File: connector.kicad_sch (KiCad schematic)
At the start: 7 parts, among them J3 Conn_01x02, J4 Conn_02x20_Counter_Clockwise

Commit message: Populate Board
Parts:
- removed J3: Conn_01x02, TerminalBlock_Phoenix:TerminalBlock_Phoenix_PT-1,5-2-5.0-H_1x02_P5.00mm_Horizontal, symbol Connector_Generic:Conn_01x02
- removed JP10, JP6, JP7, JP8, JP9: SolderJumper_2_Bridged, Jumper:SolderJumper-2_P1.3mm_Bridged_Pad1.0x1.5mm, symbol Jumper:SolderJumper_2_Bridged
- renumbered J4 to J5
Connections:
- net PROTO-1 is gone; now on net Flex_Sensor: J5.27 (Pin_27)
- net PROTO-2 is gone; now on net FAN-OUT: J5.29 (Pin_29)
- net PROTO-3 is gone; now on net FUELPUMP-OUT: J5.31 (Pin_31)
- net PROTO-4 is gone; now on net TACHO-OUT: J5.33 (Pin_33)
- net PROTO-5 is gone; now on net Clutch_in: J5.35 (Pin_35)
- net HC-1-OUT: now also J5.9 (Pin_9); no longer J5.10 (Pin_10)
- net HC-2-OUT: now also J5.10 (Pin_10); no longer J5.6 (Pin_6)
- net IDLE-OUT: now also J5.11 (Pin_11); no longer J5.8 (Pin_8)
- net INJ-3-OUT: now also J5.6 (Pin_6); no longer J5.7 (Pin_7)
- net INJ-4-OUT: now also J5.7 (Pin_7), J5.8 (Pin_8); no longer J5.11 (Pin_11), J5.9 (Pin_9)
- net VDDA renamed +5VA
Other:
- note added: "To Fix"

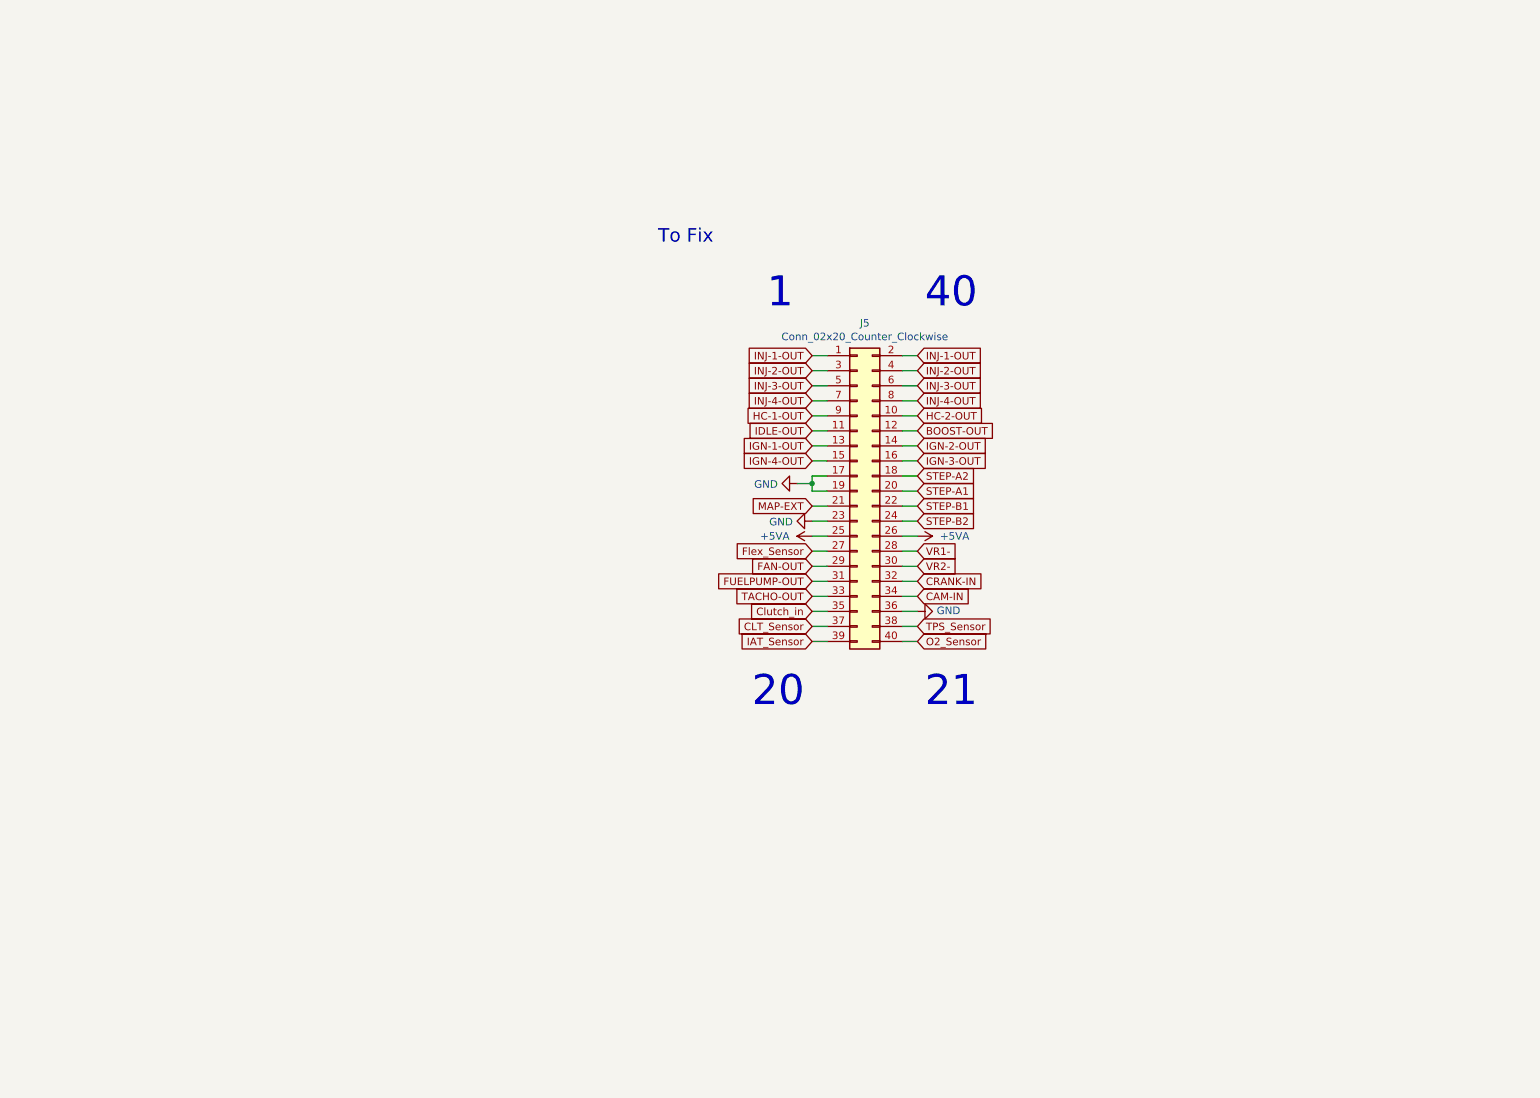
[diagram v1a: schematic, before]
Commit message: Add additional IOs
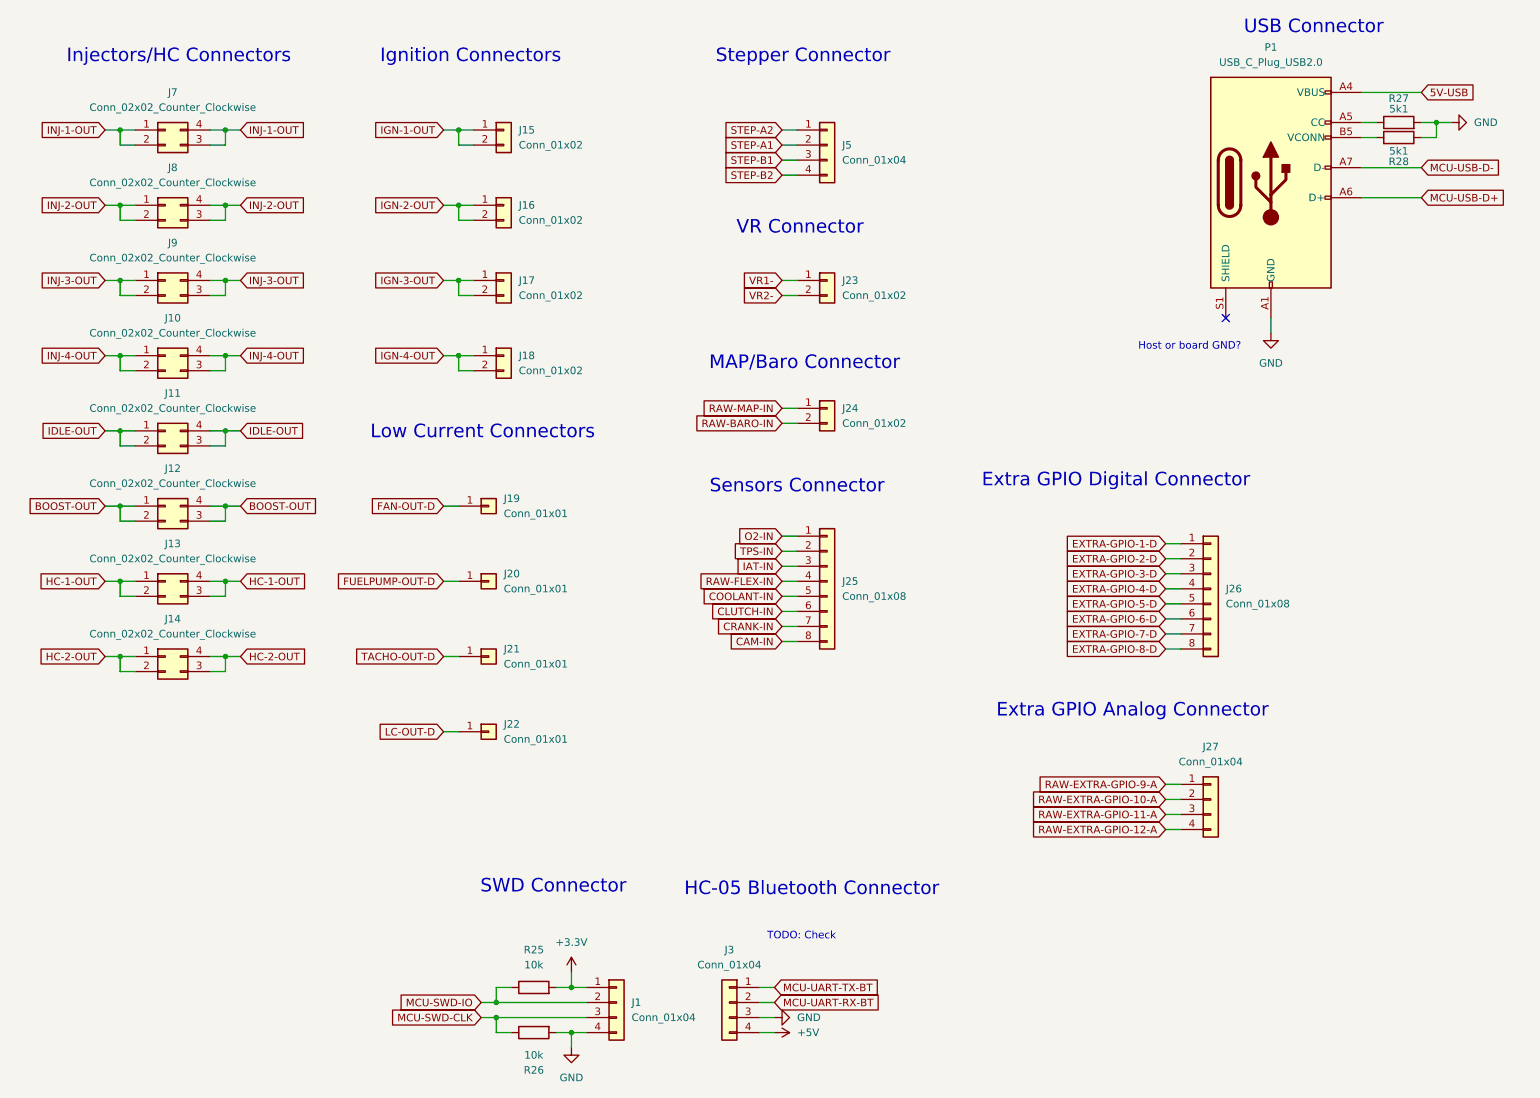
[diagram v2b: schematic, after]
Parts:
- removed J5: Conn_02x20_Counter_Clockwise, Connector_IDC:IDC-Header_2x20_P2.54mm_Vertical, symbol Connector_Generic:Conn_02x20_Odd_Even
- added J1, J27, J3, J5: Conn_01x04, Connector_PinHeader_2.54mm:PinHeader_1x04_P2.54mm_Vertical, symbol Connector_Generic:Conn_01x04
- added J10, J11, J12, J13, J14, J7, J8, J9: Conn_02x02_Counter_Clockwise, Connector_PinHeader_2.54mm:PinHeader_2x02_P2.54mm_Vertical, symbol Connector_Generic:Conn_02x02_Counter_Clockwise
- added J15, J16, J17, J18, J23, J24: Conn_01x02, Connector_PinHeader_2.54mm:PinHeader_1x02_P2.54mm_Vertical, symbol Connector_Generic:Conn_01x02
- added J19, J20, J21, J22: Conn_01x01, Connector_PinHeader_2.54mm:PinHeader_1x01_P2.54mm_Vertical, symbol Connector_Generic:Conn_01x01
- added J25, J26: Conn_01x08, Connector_PinHeader_2.54mm:PinHeader_1x08_P2.54mm_Vertical, symbol Connector_Generic:Conn_01x08
- added P1: USB_C_Plug_USB2.0, Connector_USB:USB_C_Receptacle_Palconn_UTC16-G, symbol Connector:USB_C_Plug_USB2.0
- added R25, R26: 10k, Resistor_SMD:R_0805_2012Metric, symbol Device:R
- added R27, R28: 5k1, Resistor_SMD:R_0805_2012Metric, symbol Device:R
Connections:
- net BOOST-OUT: now also J12.1 (Pin_1), J12.2 (Pin_2), J12.3 (Pin_3), J12.4 (Pin_4)
- net CAM-IN: now also J25.8 (Pin_8)
- net CRANK-IN: now also J25.7 (Pin_7)
- net GND: now also J1.4 (Pin_4), J3.3 (Pin_3), P1.A1 (GND), P1.A12 (GND), P1.B1 (GND), P1.B12 (GND), R26.2, R27.2, R28.1
- net HC-1-OUT: now also J13.1 (Pin_1), J13.2 (Pin_2), J13.3 (Pin_3), J13.4 (Pin_4)
- net HC-2-OUT: now also J14.1 (Pin_1), J14.2 (Pin_2), J14.3 (Pin_3), J14.4 (Pin_4)
- net IDLE-OUT: now also J11.1 (Pin_1), J11.2 (Pin_2), J11.3 (Pin_3), J11.4 (Pin_4)
- net IGN-1-OUT: now also J15.1 (Pin_1), J15.2 (Pin_2)
- net IGN-2-OUT: now also J16.1 (Pin_1), J16.2 (Pin_2)
- net IGN-3-OUT: now also J17.1 (Pin_1), J17.2 (Pin_2)
- net IGN-4-OUT: now also J18.1 (Pin_1), J18.2 (Pin_2)
- net INJ-1-OUT: now also J7.1 (Pin_1), J7.2 (Pin_2), J7.3 (Pin_3), J7.4 (Pin_4)
- net INJ-2-OUT: now also J8.1 (Pin_1), J8.2 (Pin_2), J8.3 (Pin_3), J8.4 (Pin_4)
- net INJ-3-OUT: now also J9.1 (Pin_1), J9.2 (Pin_2), J9.3 (Pin_3), J9.4 (Pin_4)
- net INJ-4-OUT: now also J10.1 (Pin_1), J10.2 (Pin_2), J10.3 (Pin_3), J10.4 (Pin_4)
- net STEP-A1: now also J5.2 (Pin_2)
- net STEP-A2: now also J5.1 (Pin_1)
- net STEP-B1: now also J5.3 (Pin_3)
- net STEP-B2: now also J5.4 (Pin_4)
- net VR1-: now also J23.1 (Pin_1)
- net VR2-: now also J23.2 (Pin_2)
- new net: P1.A5 (CC), R27.1
- new net: P1.B5 (VCONN), R28.2
- new net +3.3V: J1.1 (Pin_1), R25.2
- new net +5V: J3.4 (Pin_4)
- new net 5V-USB: P1.A4 (VBUS), P1.A9 (VBUS), P1.B4 (VBUS), P1.B9 (VBUS)
- new net CLUTCH-IN: J25.6 (Pin_6)
- new net COOLANT-IN: J25.5 (Pin_5)
- new net EXTRA-GPIO-1-D: J26.1 (Pin_1)
- new net EXTRA-GPIO-2-D: J26.2 (Pin_2)
- new net EXTRA-GPIO-3-D: J26.3 (Pin_3)
- new net EXTRA-GPIO-4-D: J26.4 (Pin_4)
- new net EXTRA-GPIO-5-D: J26.5 (Pin_5)
- new net EXTRA-GPIO-6-D: J26.6 (Pin_6)
- new net EXTRA-GPIO-7-D: J26.7 (Pin_7)
- new net EXTRA-GPIO-8-D: J26.8 (Pin_8)
- new net FAN-OUT-D: J19.1 (Pin_1)
- new net FUELPUMP-OUT-D: J20.1 (Pin_1)
- new net IAT-IN: J25.3 (Pin_3)
- new net LC-OUT-D: J22.1 (Pin_1)
- new net MCU-SWD-CLK: J1.3 (Pin_3), R26.1
- new net MCU-SWD-IO: J1.2 (Pin_2), R25.1
- new net MCU-UART-RX-BT: J3.2 (Pin_2)
- new net MCU-UART-TX-BT: J3.1 (Pin_1)
- new net MCU-USB-D+: P1.A6 (D+)
- new net MCU-USB-D-: P1.A7 (D-)
- new net O2-IN: J25.1 (Pin_1)
- new net RAW-BARO-IN: J24.2 (Pin_2)
- new net RAW-EXTRA-GPIO-10-A: J27.2 (Pin_2)
- new net RAW-EXTRA-GPIO-11-A: J27.3 (Pin_3)
- new net RAW-EXTRA-GPIO-12-A: J27.4 (Pin_4)
- new net RAW-EXTRA-GPIO-9-A: J27.1 (Pin_1)
- new net RAW-FLEX-IN: J25.4 (Pin_4)
- new net RAW-MAP-IN: J24.1 (Pin_1)
- new net TACHO-OUT-D: J21.1 (Pin_1)
- new net TPS-IN: J25.2 (Pin_2)
- no-connect marks 0 -> 1
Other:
- note added: "Extra GPIO Analog Connector"
- note added: "Extra GPIO Digital Connector"
- note added: "HC-05 Bluetooth Connector"
- note added: "Host or board GND?"
- note added: "Ignition Connectors"
- note added: "Injectors/HC Connectors"
- note added: "Low Current Connectors"
- note added: "MAP/Baro Connector"
- note added: "SWD Connector"
- note added: "Sensors Connector"
- note added: "Stepper Connector"
- note added: "TODO: Check"
- note added: "USB Connector"
- note added: "VR Connector"
- note removed: "1"
- note removed: "20"
- note removed: "21"
- note removed: "40"
- note removed: "To Fix"

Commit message: Pre MCU switch
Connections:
- net CLUTCH-IN: now also J25.3 (Pin_3); no longer J25.6 (Pin_6)
- net COOLANT-IN: now also J25.6 (Pin_6); no longer J25.5 (Pin_5)
- net IAT-IN: now also J25.2 (Pin_2); no longer J25.3 (Pin_3)
- net O2-IN: now also J25.5 (Pin_5); no longer J25.1 (Pin_1)
- net RAW-FLEX-IN: now also J25.1 (Pin_1); no longer J25.4 (Pin_4)
- net TPS-IN: now also J25.4 (Pin_4); no longer J25.2 (Pin_2)
- net EXTRA-GPIO-1-D renamed MCU-EXTRA-GPIO-1-D
- net EXTRA-GPIO-2-D renamed MCU-EXTRA-GPIO-2-D
- net EXTRA-GPIO-3-D renamed MCU-EXTRA-GPIO-3-D
- net EXTRA-GPIO-4-D renamed MCU-EXTRA-GPIO-4-D
- net EXTRA-GPIO-5-D renamed MCU-EXTRA-GPIO-5-D
- net EXTRA-GPIO-6-D renamed MCU-EXTRA-GPIO-6-D
- net EXTRA-GPIO-7-D renamed MCU-EXTRA-GPIO-7-D
- net EXTRA-GPIO-8-D renamed MCU-EXTRA-GPIO-8-D
- net MCU-UART-RX-BT renamed MCU-UART-BT-RX
- net MCU-UART-TX-BT renamed MCU-UART-BT-TX

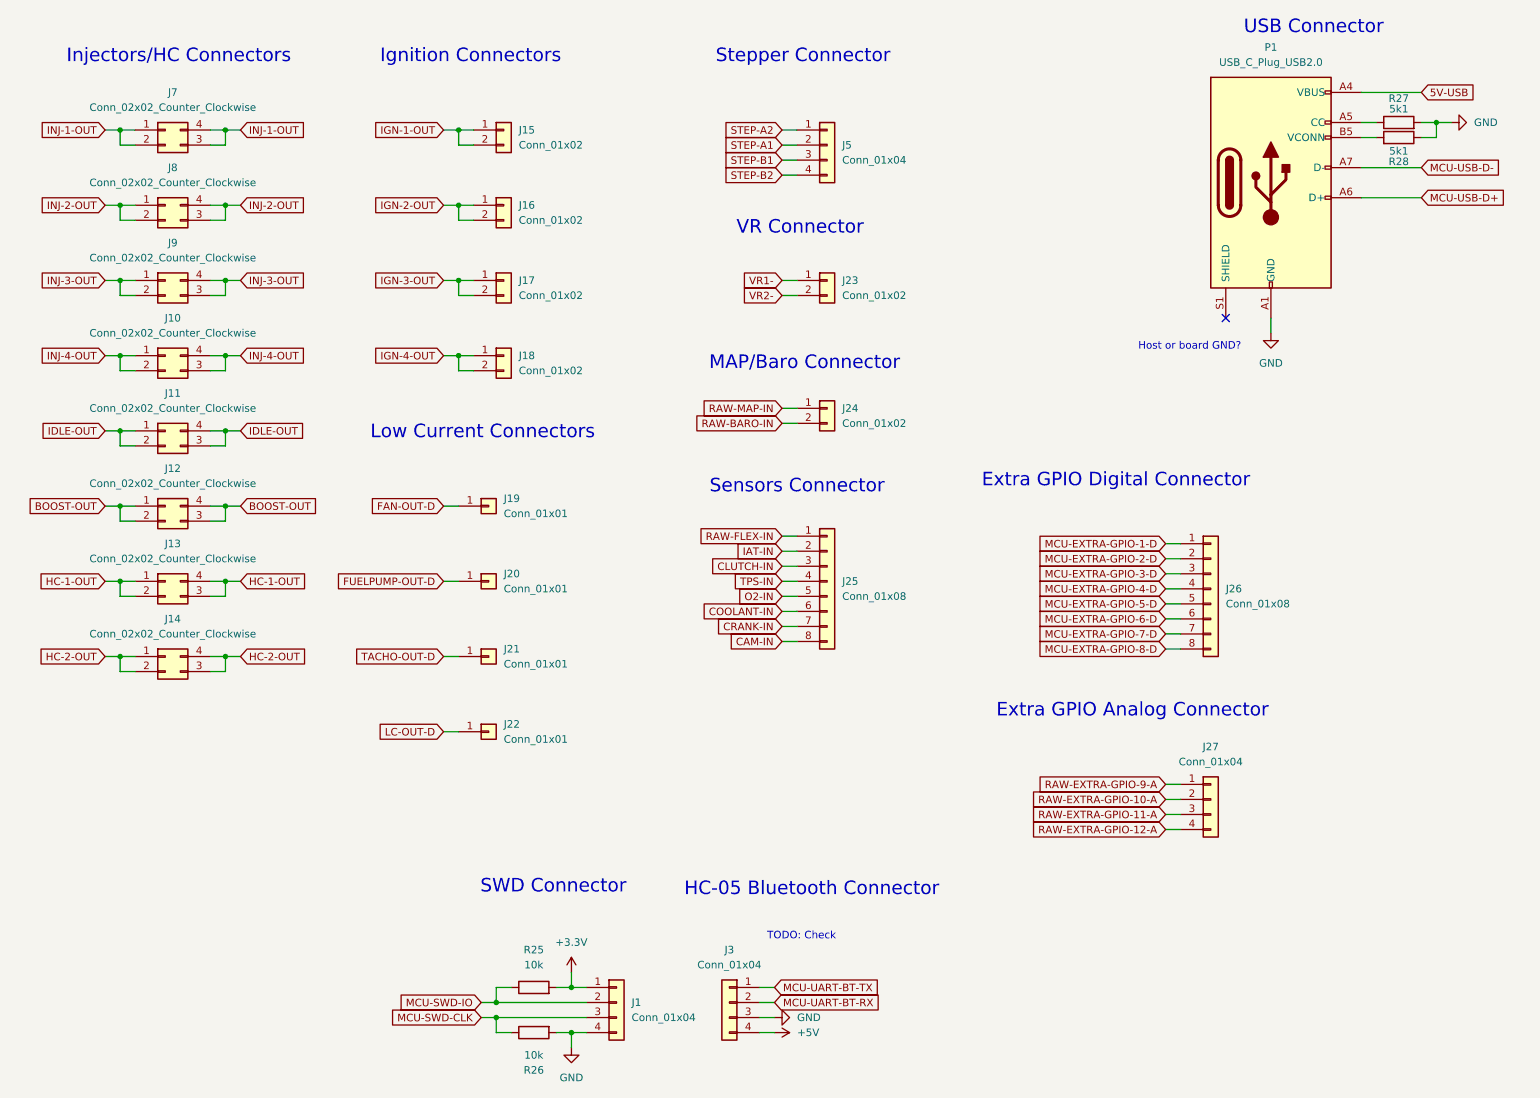
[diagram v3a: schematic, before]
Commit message: Update from Speeduino Discord suggestions (thanks to Detonator)
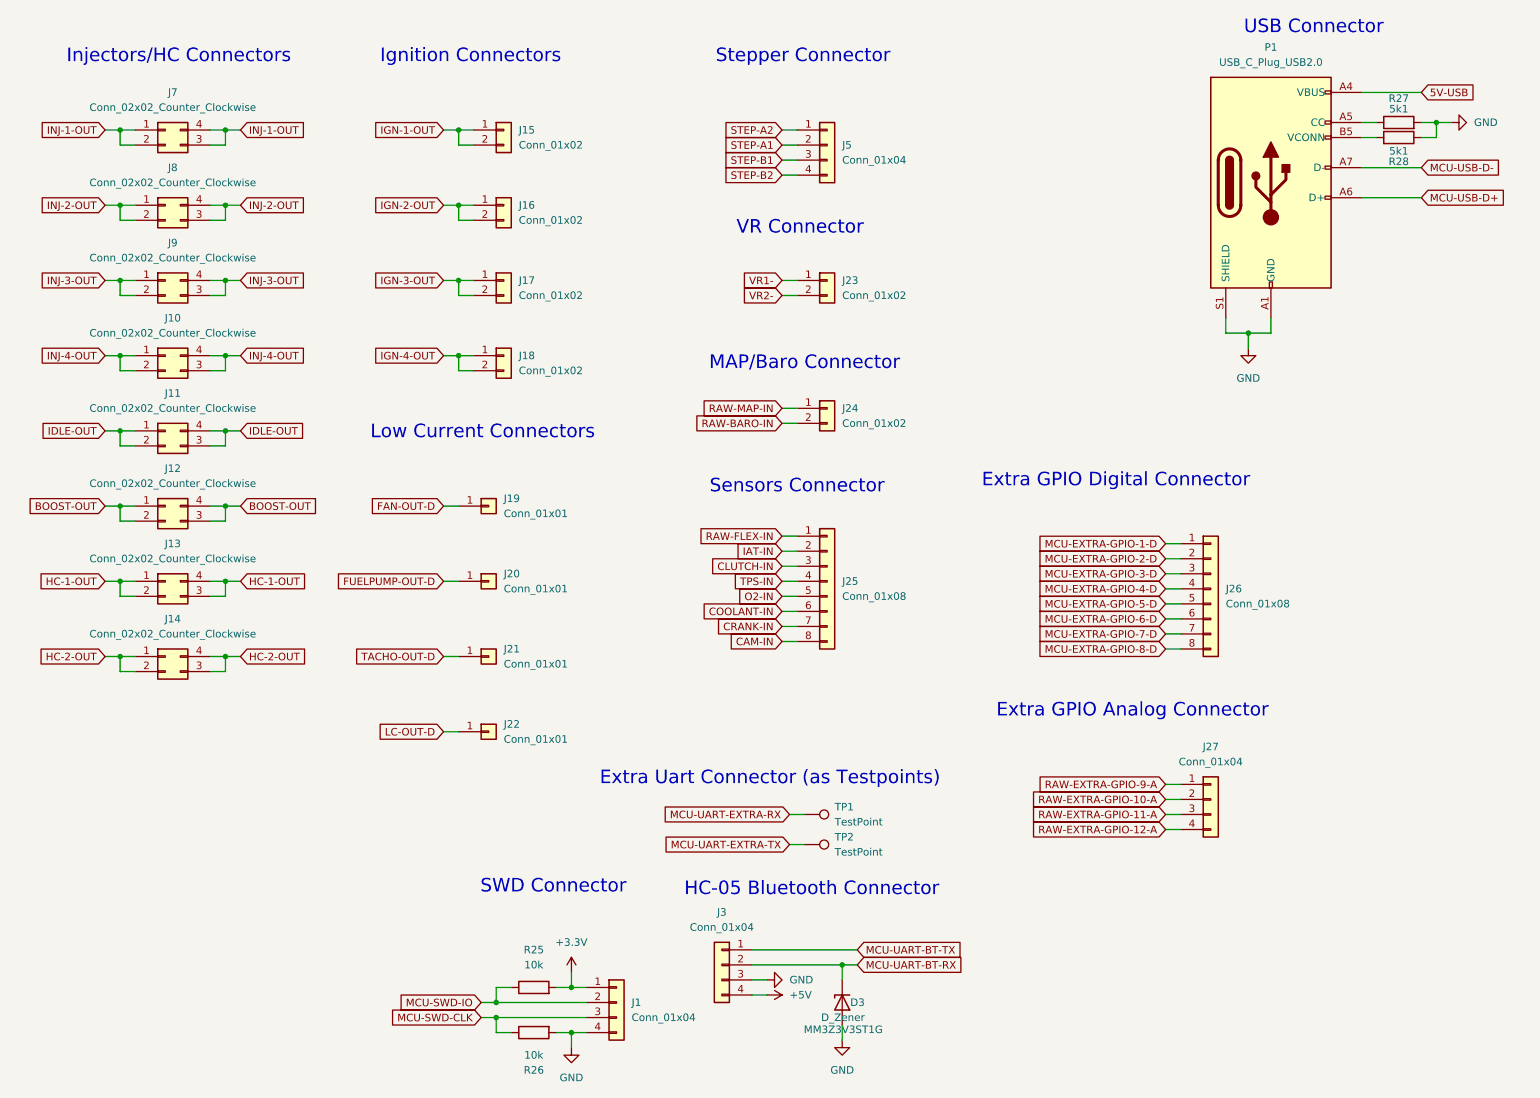
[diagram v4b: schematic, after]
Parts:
- added D3: D_Zener, Diode_SMD:D_SOD-323, symbol Device:D_Zener
- added TP1, TP2: TestPoint, TestPoint:TestPoint_Pad_D1.0mm, symbol Connector:TestPoint
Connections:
- net GND: now also P1.S1 (SHIELD), D3.2 (A)
- net MCU-UART-BT-RX: now also D3.1 (K)
- new net MCU-UART-EXTRA-RX: TP1.1
- new net MCU-UART-EXTRA-TX: TP2.1
- no-connect marks 1 -> 0
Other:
- note added: "Extra Uart Connector (as Testpoints)"
- note removed: "Host or board GND?"
- note removed: "TODO: Check"
- moved on the sheet: J3
